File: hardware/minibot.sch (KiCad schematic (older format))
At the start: 44 parts, among them J1 USB_OTG, J2 SWD, J3 RESET, J4 BAUD, J5 CONN_01X18, SW1 BOOT, SW2 RESET, U1 TLV70233DBV, U2 TLV70228DBV, U3 OV7690-R20A, U4 RN41, U5 LSM6DS3US

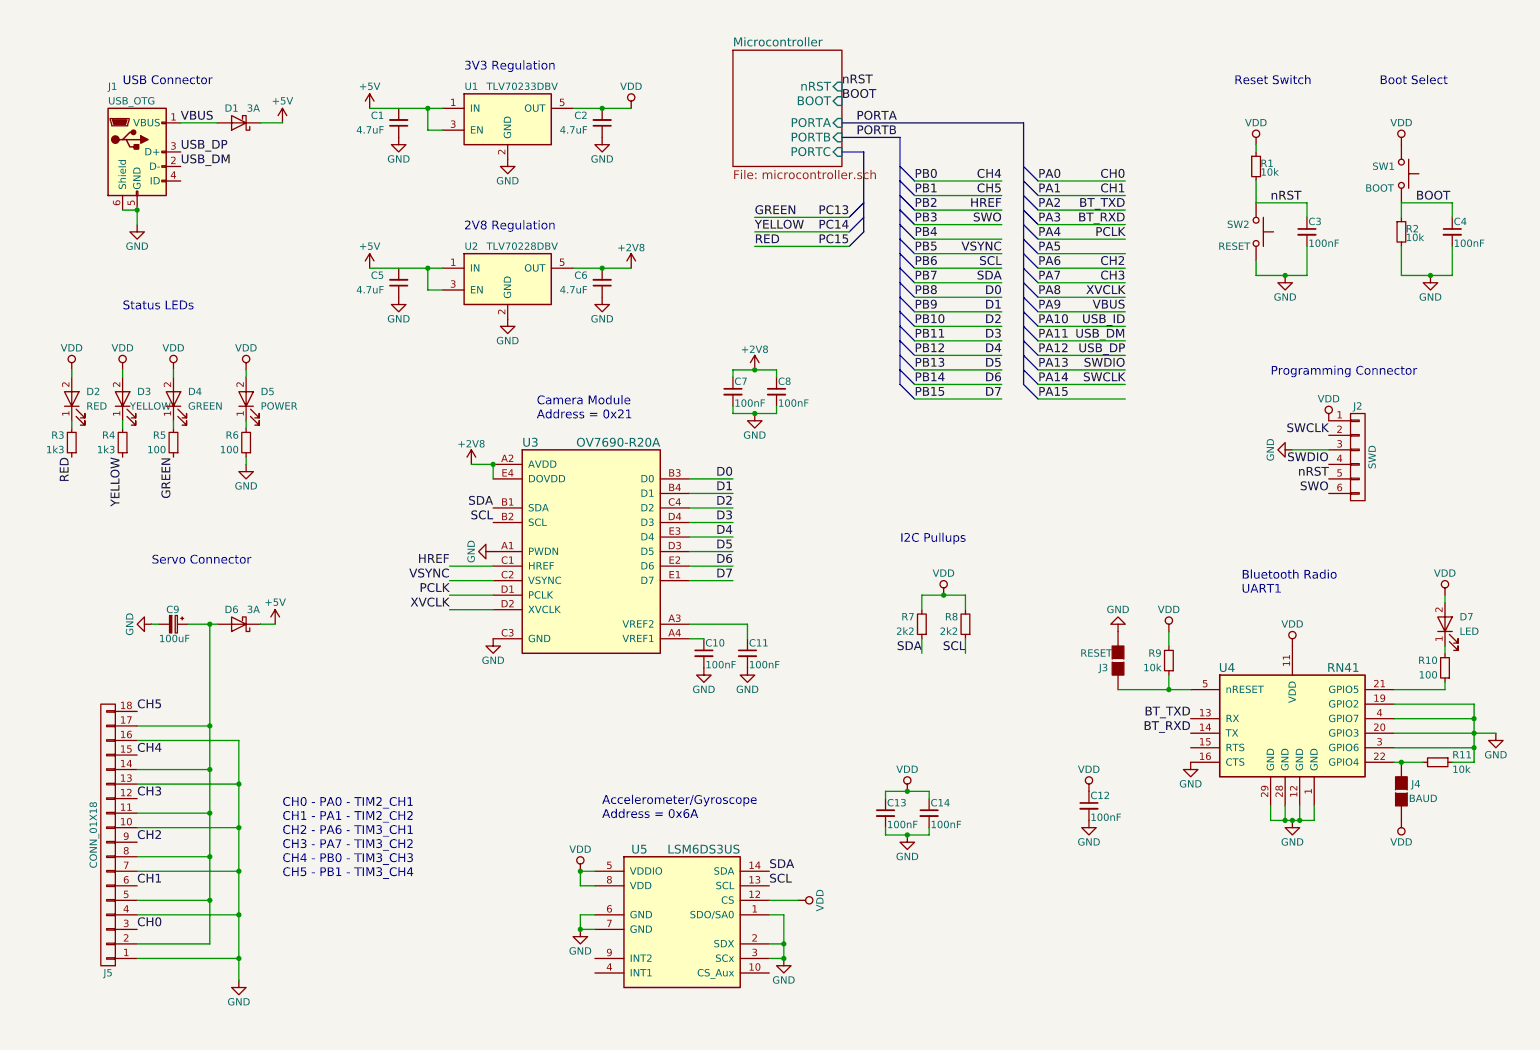
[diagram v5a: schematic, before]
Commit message: Add in some logic level translation for the camera signals. Update the annotations and plot the PDF
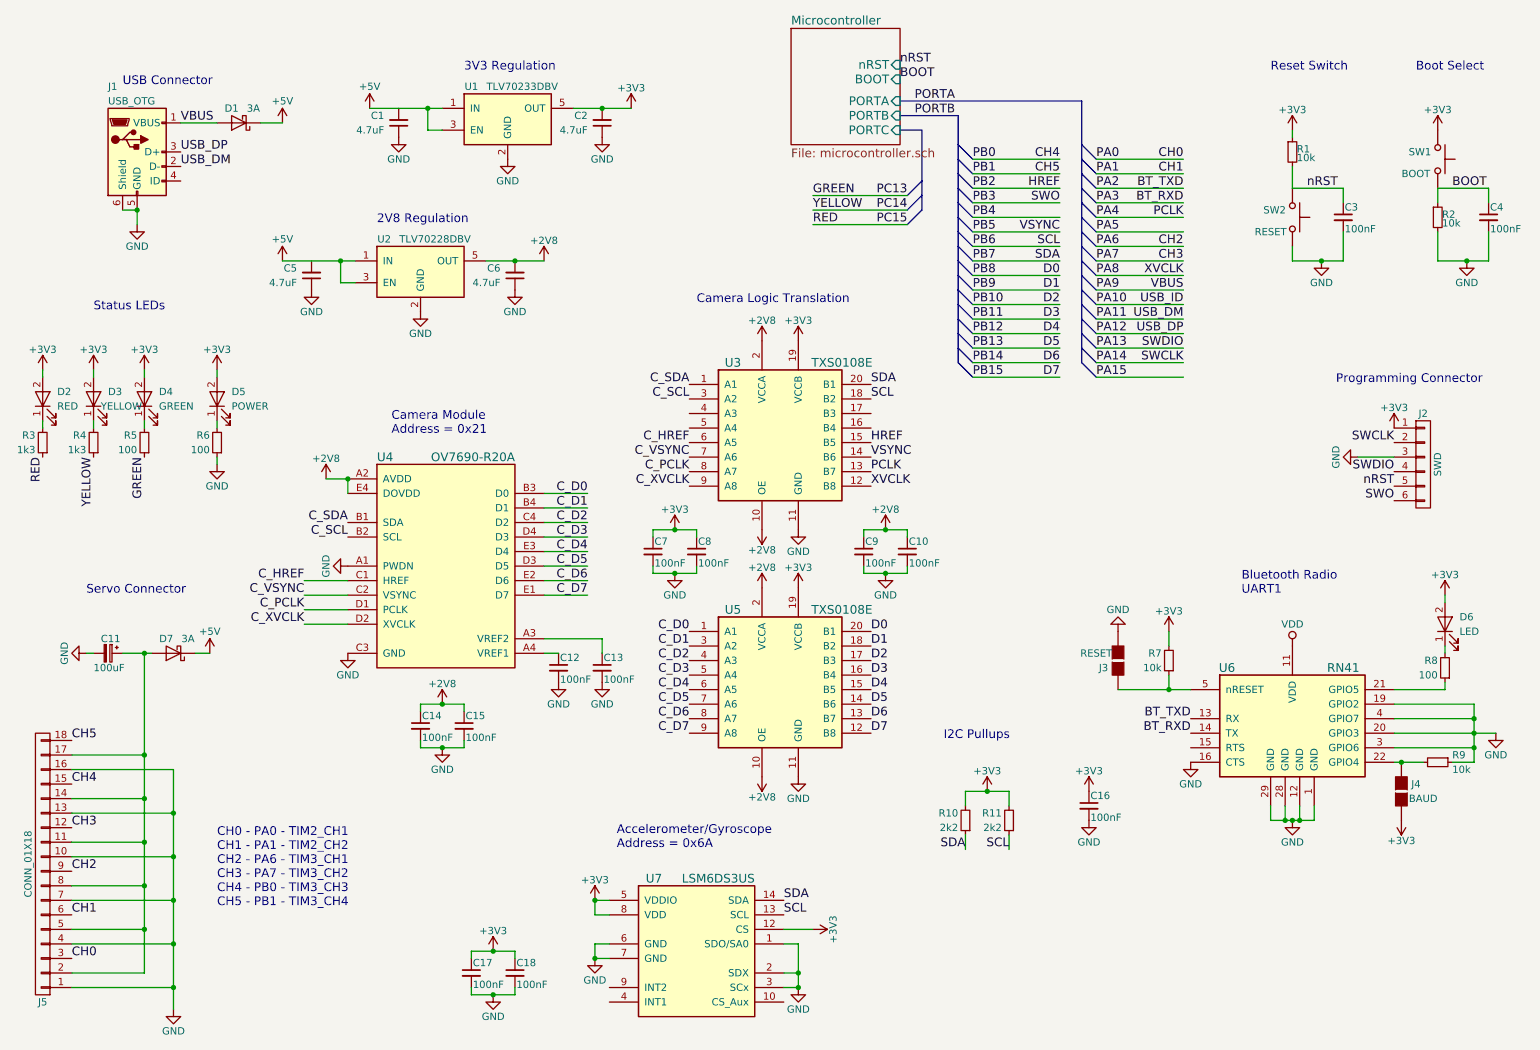
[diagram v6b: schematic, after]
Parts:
- added C10, C7, C8, C9: 100nF, Capacitors_SMD:C_0603, symbol C_Small
- added U3, U5: TXS0108E, symbol TXS0108E
- renumbered C9 to C11, C10 to C12, C11 to C13, C7 to C14, C8 to C15, C12 to C16, C13 to C17, C14 to C18, D7 to D6, D6 to D7, R7 to R10, R8 to R11, R9 to R7, R10 to R8, R11 to R9, U3 to U4, U4 to U6, U5 to U7
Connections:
- net +2V8: now also C10.1, C9.1, U3.10 (OE), U3.2 (VCCA), U5.10 (OE), U5.2 (VCCA)
- net D0: now also U5.20 (B1); no longer U4.B3 (D0)
- net D1: now also U5.18 (B2); no longer U4.B4 (D1)
- net D2: now also U5.17 (B3); no longer U4.C4 (D2)
- net D3: now also U5.16 (B4); no longer U4.D4 (D3)
- net D4: now also U5.15 (B5); no longer U4.E3 (D4)
- net D5: now also U5.14 (B6); no longer U4.D3 (D5)
- net D6: now also U5.13 (B7); no longer U4.E2 (D6)
- net D7: now also U5.12 (B8); no longer U4.E1 (D7)
- net GND: now also C10.2, C7.2, C8.2, C9.2, U3.11 (GND), U5.11 (GND)
- net HREF: now also U3.15 (B5); no longer U4.C1 (HREF)
- net PA4: now also U3.13 (B7); no longer U4.D1 (PCLK)
- net PA8: now also U3.12 (B8); no longer U4.D2 (XVCLK)
- net PB5: now also U3.14 (B6); no longer U4.C2 (VSYNC)
- net PB6: now also U3.18 (B2); no longer U4.B2 (SCL)
- net PB7: now also U3.20 (B1); no longer U4.B1 (SDA)
- net VDD: no longer C16.1, C17.1, C18.1, C2.2, D2.2 (A), D3.2 (A), D4.2 (A), D5.2 (A), D6.2 (A), J2.1 (P1), J4.2 (G2), R1.1, R10.2, R11.2, R7.2, SW1.1, U1.5 (OUT), U7.12 (CS), U7.5 (VDDIO), U7.8 (VDD)
- new net +3V3: C16.1, C17.1, C18.1, C2.2, C7.1, C8.1, D2.2 (A), D3.2 (A), D4.2 (A), D5.2 (A), D6.2 (A), J2.1 (P1), J4.2 (G2), R1.1, R10.2, R11.2, R7.2, SW1.1, U1.5 (OUT), U3.19 (VCCB), U5.19 (VCCB), U7.12 (CS), U7.5 (VDDIO), U7.8 (VDD)
- new net C_D0: U4.B3 (D0), U5.1 (A1)
- new net C_D1: U4.B4 (D1), U5.3 (A2)
- new net C_D2: U4.C4 (D2), U5.4 (A3)
- new net C_D3: U4.D4 (D3), U5.5 (A4)
- new net C_D4: U4.E3 (D4), U5.6 (A5)
- new net C_D5: U4.D3 (D5), U5.7 (A6)
- new net C_D6: U4.E2 (D6), U5.8 (A7)
- new net C_D7: U4.E1 (D7), U5.9 (A8)
- new net C_HREF: U3.6 (A5), U4.C1 (HREF)
- new net C_PCLK: U3.8 (A7), U4.D1 (PCLK)
- new net C_SCL: U3.3 (A2), U4.B2 (SCL)
- new net C_SDA: U3.1 (A1), U4.B1 (SDA)
- new net C_VSYNC: U3.7 (A6), U4.C2 (VSYNC)
- new net C_XVCLK: U3.9 (A8), U4.D2 (XVCLK)
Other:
- note added: "Camera Logic Translation"
- moved on the sheet: C11, C12, C13, C14, C15, C17, C18, C3, C4, C5, C6, D2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

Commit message: Remove the camera from the schematic as it's no longer a reasonable goal
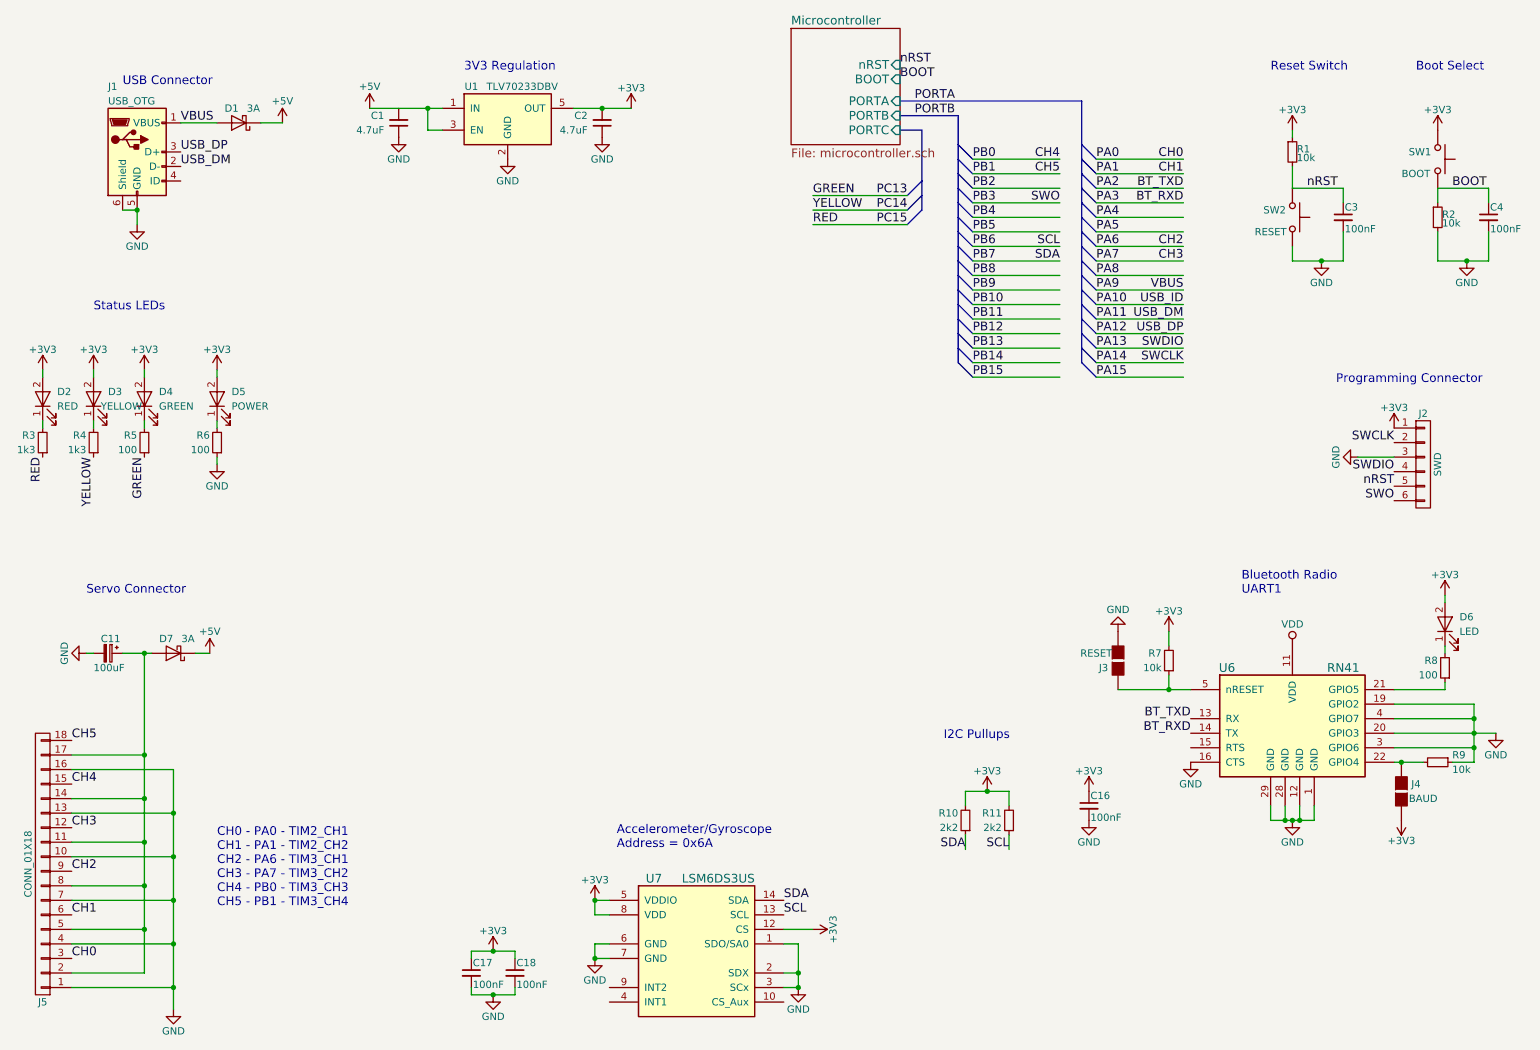
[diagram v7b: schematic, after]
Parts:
- removed C10, C12, C13, C14, C15, C7, C8, C9: 100nF, Capacitors_SMD:C_0603, symbol C_Small
- removed C5, C6: 4.7uF, Capacitors_SMD:C_0805, symbol C_Small
- removed U2: TLV70228DBV, TO_SOT_Packages_SMD:SOT-23-5, symbol TLV70228DBV
- removed U3, U5: TXS0108E, symbol TXS0108E
- removed U4: OV7690-R20A, symbol OV7690-R20A
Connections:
- net labels removed: +2V8, C_D0, C_D1, C_D2, C_D3, C_D4, C_D5, C_D6, C_D7, C_HREF, C_PCLK, C_SCL, C_SDA, C_VSYNC, C_XVCLK, D0, D1, D2, D3, D4, D5, D6, D7, HREF, PCLK, VSYNC, XVCLK
- wire segments 200 -> 153
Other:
- note removed: "2V8 Regulation\n"
- note removed: "Camera Logic Translation"
- note removed: "Camera Module\nAddress = 0x21\n"

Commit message: Start adjusting the signals now that the camera isn't in the way
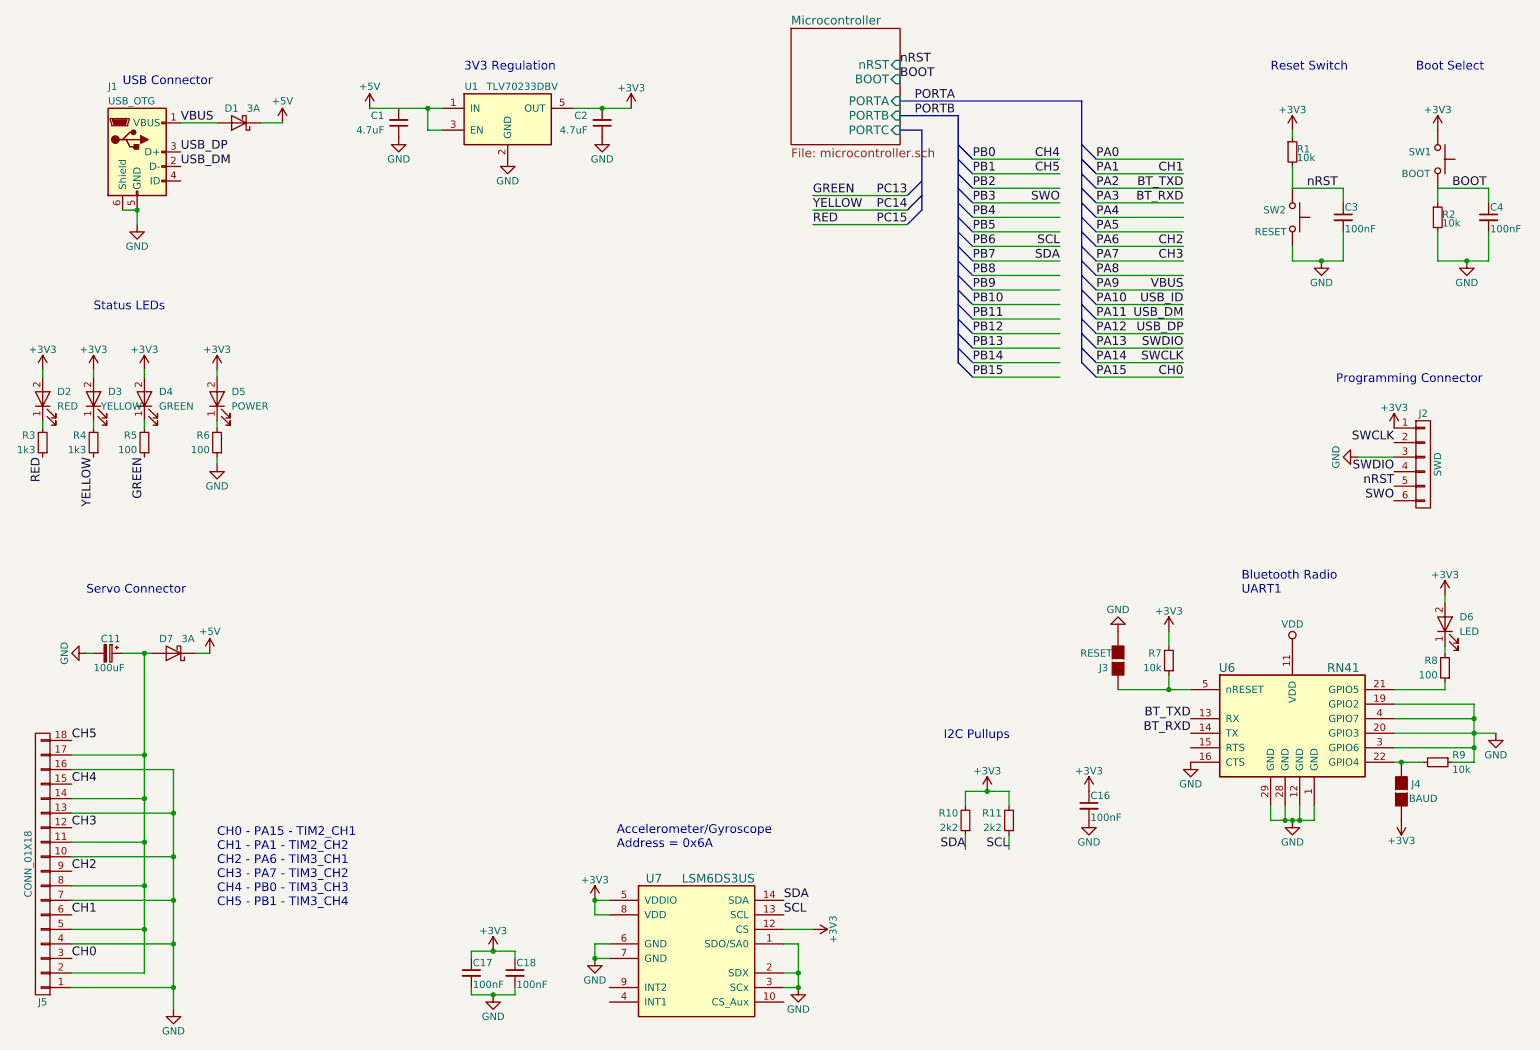
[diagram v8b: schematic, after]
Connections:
- wire segments 153 -> 125
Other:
- note added: "CH0 - PA15 - TIM2_CH1\nCH1 - PA1 - TIM2_CH2\nCH2 - PA6 - TIM3_CH1\nCH3 - PA7 - TIM3_CH2\nCH4 - PB0 - TIM3_CH3\nCH5 - PB1 - TIM3_CH4"
- note removed: "CH0 - PA0 - TIM2_CH1\nCH1 - PA1 - TIM2_CH2\nCH2 - PA6 - TIM3_CH1\nCH3 - PA7 - TIM3_CH2\nCH4 - PB0 - TIM3_CH3\nCH5 - PB1 - TIM3_CH4"
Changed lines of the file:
@@
 Text Label 8700 1850 2    60   ~ 0
 BT_RXD
-Text Label 8700 1550 2    60   ~ 0
+Text Label 8700 3050 2    60   ~ 0
 CH0
 Text Label 8700 1650 2    60   ~ 0
@@
 	9800 2250 9800 2050
 Wire Wire Line
-	9450 2250 9650 2250
-Wire Wire Line
-	9650 2250 9800 2250
+	9450 2250 9800 2250
 Connection ~ 9650 2250
 Wire Wire Line
@@
 	10800 2250 10800 2050
 Wire Wire Line
-	10450 2250 10650 2250
-Wire Wire Line
-	10650 2250 10800 2250
+	10450 2250 10800 2250
 Connection ~ 10650 2250
 Wire Wire Line
@@
 	10700 5700 10550 5700
 Wire Wire Line
-	10700 5300 10700 5400
-Wire Wire Line
-	10700 5400 10700 5500
-Wire Wire Line
-	10700 5500 10700 5600
-Wire Wire Line
-	10700 5600 10700 5700
+	10700 5300 10700 5700
 Wire Wire Line
 	10150 5600 10700 5600
 Connection ~ 10700 5600
 Wire Wire Line
-	10150 5500 10700 5500
-Wire Wire Line
-	10700 5500 10850 5500
+	10150 5500 10850 5500
 Wire Wire Line
 	10150 5400 10700 5400
 Connection ~ 10700 5500
 Wire Wire Line
-	10150 5700 10200 5700
-Wire Wire Line
-	10200 5700 10350 5700
+	10150 5700 10350 5700
 Connection ~ 10200 5700
 Wire Wire Line
@@
 	9600 6100 9600 6000
 Wire Wire Line
-	9300 6100 9400 6100
-Wire Wire Line
-	9400 6100 9450 6100
-Wire Wire Line
-	9450 6100 9500 6100
-Wire Wire Line
-	9500 6100 9600 6100
+	9300 6100 9600 6100
 Wire Wire Line
 	9300 6100 9300 6000
@@
 Connection ~ 9500 6100
 Wire Wire Line
-	8250 5200 8600 5200
-Wire Wire Line
-	8600 5200 8750 5200
+	8250 5200 8750 5200
 Wire Wire Line
 	8600 5100 8600 5200
@@
 	1550 7150 1050 7150
 Wire Wire Line
-	1550 4950 1550 5650
-Wire Wire Line
-	1550 5650 1550 5950
-Wire Wire Line
-	1550 5950 1550 6250
-Wire Wire Line
-	1550 6250 1550 6550
-Wire Wire Line
-	1550 6550 1550 6850
-Wire Wire Line
-	1550 6850 1550 7150
+	1550 4950 1550 7150
 Wire Wire Line
 	1050 6850 1550 6850
@@
 	2350 1300 2500 1300
 Wire Wire Line
-	1750 5750 1750 6050
-Wire Wire Line
-	1750 6050 1750 6350
-Wire Wire Line
-	1750 6350 1750 6650
-Wire Wire Line
-	1750 6650 1750 6950
-Wire Wire Line
-	1750 6950 1750 7250
-Wire Wire Line
-	1750 7250 1750 7400
+	1750 5750 1750 7400
 Wire Wire Line
 	1500 1900 1400 1900
@@
 	1900 4950 2000 4950
 Wire Wire Line
-	1400 4950 1550 4950
-Wire Wire Line
-	1550 4950 1600 4950
-Wire Wire Line
-	4500 1200 4700 1200
-Wire Wire Line
-	4700 1200 4900 1200
+	1400 4950 1600 4950
+Wire Wire Line
+	4500 1200 4900 1200
 Connection ~ 4700 1200
 Wire Bus Line
@@
 	6750 1250 7150 1250
 Wire Bus Line
-	7150 1250 7150 1450
-Wire Bus Line
-	7150 1450 7150 1550
-Wire Bus Line
-	7150 1550 7150 1650
-Wire Bus Line
-	7150 1650 7150 1750
-Wire Bus Line
-	7150 1750 7150 1850
-Wire Bus Line
-	7150 1850 7150 1950
-Wire Bus Line
-	7150 1950 7150 2050
-Wire Bus Line
-	7150 2050 7150 2150
-Wire Bus Line
-	7150 2150 7150 2250
-Wire Bus Line
-	7150 2250 7150 2350
-Wire Bus Line
-	7150 2350 7150 2450
-Wire Bus Line
-	7150 2450 7150 2550
-Wire Bus Line
-	7150 2550 7150 2650
-Wire Bus Line
-	7150 2650 7150 2750
-Wire Bus Line
-	7150 2750 7150 2850
-Wire Bus Line
-	7150 2850 7150 2950
+	7150 1250 7150 2950
 Wire Wire Line
 	850  3400 850  3350
@@
 	9900 3600 10150 3600
 Wire Bus Line
-	8000 1150 8000 1450
-Wire Bus Line
-	8000 1450 8000 1550
-Wire Bus Line
-	8000 1550 8000 1650
-Wire Bus Line
-	8000 1650 8000 1750
-Wire Bus Line
-	8000 1750 8000 1850
-Wire Bus Line
-	8000 1850 8000 1950
-Wire Bus Line
-	8000 1950 8000 2050
-Wire Bus Line
-	8000 2050 8000 2150
-Wire Bus Line
-	8000 2150 8000 2250
-Wire Bus Line
-	8000 2250 8000 2350
-Wire Bus Line
-	8000 2350 8000 2450
-Wire Bus Line
-	8000 2450 8000 2550
-Wire Bus Line
-	8000 2550 8000 2650
-Wire Bus Line
-	8000 2650 8000 2750
-Wire Bus Line
-	8000 2750 8000 2850
-Wire Bus Line
-	8000 2850 8000 2950
+	8000 1150 8000 2950
 Wire Wire Line
 	7250 1550 7850 1550
@@
 $EndComp
 Wire Wire Line
-	3800 7300 3950 7300
-Wire Wire Line
-	3950 7300 4100 7300
+	3800 7300 4100 7300
 Wire Wire Line
 	4100 7300 4100 7250
@@
 	3800 7050 3800 7000
 Wire Wire Line
-	3800 7000 3950 7000
-Wire Wire Line
-	3950 7000 4100 7000
+	3800 7000 4100 7000
 Wire Wire Line
 	4100 7000 4100 7050
@@
 	5950 7150 6050 7150
 Wire Wire Line
-	6050 6950 6050 7150
-Wire Wire Line
-	6050 7150 6050 7250
+	6050 6950 6050 7250
 Connection ~ 6050 7250
 Wire Wire Line
@@
 I2C Pullups\n
 Wire Wire Line
-	7200 5900 7350 5900
-Wire Wire Line
-	7350 5900 7500 5900
+	7200 5900 7500 5900
 Connection ~ 7350 5900
 $Comp
@@
 	6750 1350 6900 1350
 Wire Bus Line
-	6900 1350 6900 1700
-Wire Bus Line
-	6900 1700 6900 1800
-Wire Bus Line
-	6900 1800 6900 1900
+	6900 1350 6900 1900
 Entry Bus Bus
 	6800 2000 6900 1900
@@
 Connection ~ 3500 1200
 Wire Wire Line
-	3100 1200 3500 1200
-Wire Wire Line
-	3500 1200 3600 1200
+	3100 1200 3600 1200
 Text Notes 2050 6700 0    60   ~ 0
-CH0 - PA0 - TIM2_CH1\nCH1 - PA1 - TIM2_CH2\nCH2 - PA6 - TIM3_CH1\nCH3 - PA7 - TIM3_CH2\nCH4 - PB0 - TIM3_CH3\nCH5 - PB1 - TIM3_CH4
+CH0 - PA15 - TIM2_CH1\nCH1 - PA1 - TIM2_CH2\nCH2 - PA6 - TIM3_CH1\nCH3 - PA7 - TIM3_CH2\nCH4 - PB0 - TIM3_CH3\nCH5 - PB1 - TIM3_CH4
 $Comp
 L GND #PWR48
